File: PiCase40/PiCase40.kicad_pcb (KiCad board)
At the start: 2 copper layers, 66 x 20 mm, 3 parts, among them J1 Conn_02x20_Odd_Even_Male, J2 Conn_02x20_Odd_Even_Female, SW1 SW_MEC_5E

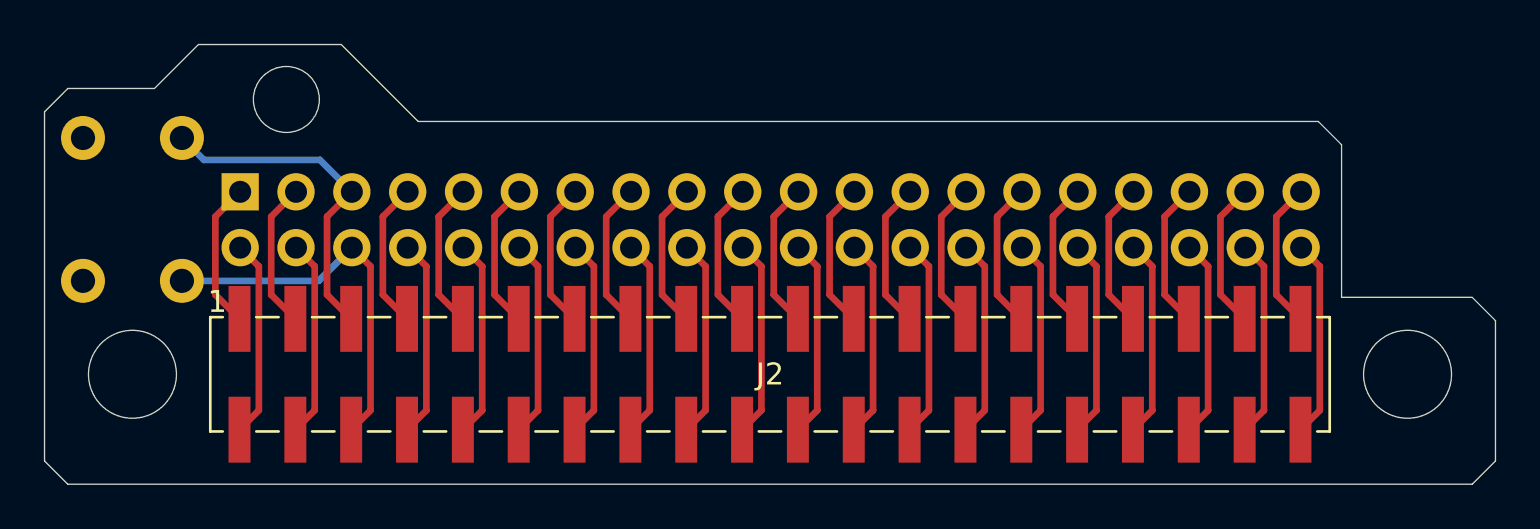
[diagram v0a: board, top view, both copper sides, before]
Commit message: Updated the PCB outline and pretified the footprints
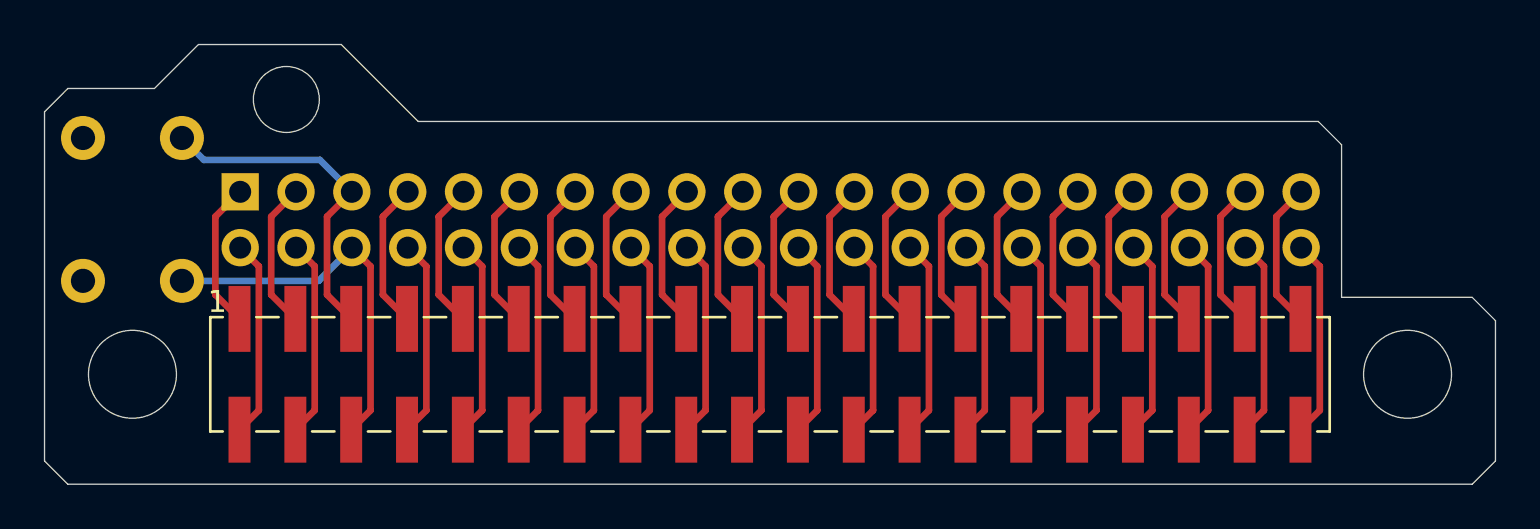
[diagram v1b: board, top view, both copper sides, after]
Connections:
- J2 pad 1: Net-(J1-Pad1) -> Net-(J2-Pad1)
- J2 pad 10: Net-(J1-Pad10) -> Net-(J2-Pad10)
- J2 pad 11: Net-(J1-Pad11) -> Net-(J2-Pad11)
- J2 pad 12: Net-(J1-Pad12) -> Net-(J2-Pad12)
- J2 pad 13: Net-(J1-Pad13) -> Net-(J2-Pad13)
- J2 pad 14: Net-(J1-Pad14) -> Net-(J2-Pad14)
- J2 pad 15: Net-(J1-Pad15) -> Net-(J2-Pad15)
- J2 pad 16: Net-(J1-Pad16) -> Net-(J2-Pad16)
- J2 pad 17: Net-(J1-Pad17) -> Net-(J2-Pad17)
- J2 pad 18: Net-(J1-Pad18) -> Net-(J2-Pad18)
- J2 pad 19: Net-(J1-Pad19) -> Net-(J2-Pad19)
- J2 pad 2: Net-(J1-Pad2) -> Net-(J2-Pad2)
- J2 pad 20: Net-(J1-Pad20) -> Net-(J2-Pad20)
- J2 pad 21: Net-(J1-Pad21) -> Net-(J2-Pad21)
- J2 pad 22: Net-(J1-Pad22) -> Net-(J2-Pad22)
- J2 pad 23: Net-(J1-Pad23) -> Net-(J2-Pad23)
- J2 pad 24: Net-(J1-Pad24) -> Net-(J2-Pad24)
- J2 pad 25: Net-(J1-Pad25) -> Net-(J2-Pad25)
- J2 pad 26: Net-(J1-Pad26) -> Net-(J2-Pad26)
- J2 pad 27: Net-(J1-Pad27) -> Net-(J2-Pad27)
- J2 pad 28: Net-(J1-Pad28) -> Net-(J2-Pad28)
- J2 pad 29: Net-(J1-Pad29) -> Net-(J2-Pad29)
- J2 pad 3: Net-(J1-Pad3) -> Net-(J2-Pad3)
- J2 pad 30: Net-(J1-Pad30) -> Net-(J2-Pad30)
- J2 pad 31: Net-(J1-Pad31) -> Net-(J2-Pad31)
- J2 pad 32: Net-(J1-Pad32) -> Net-(J2-Pad32)
- J2 pad 33: Net-(J1-Pad33) -> Net-(J2-Pad33)
- J2 pad 34: Net-(J1-Pad34) -> Net-(J2-Pad34)
- J2 pad 35: Net-(J1-Pad35) -> Net-(J2-Pad35)
- J2 pad 36: Net-(J1-Pad36) -> Net-(J2-Pad36)
- J2 pad 37: Net-(J1-Pad37) -> Net-(J2-Pad37)
- J2 pad 38: Net-(J1-Pad38) -> Net-(J2-Pad38)
- J2 pad 39: Net-(J1-Pad39) -> Net-(J2-Pad39)
- J2 pad 4: Net-(J1-Pad4) -> Net-(J2-Pad4)
- J2 pad 40: Net-(J1-Pad40) -> Net-(J2-Pad40)
- J2 pad 5: /5 -> Net-(J2-Pad5)
- J2 pad 6: /6 -> Net-(J2-Pad6)
- J2 pad 7: Net-(J1-Pad7) -> Net-(J2-Pad7)
- J2 pad 8: Net-(J1-Pad8) -> Net-(J2-Pad8)
- J2 pad 9: Net-(J1-Pad9) -> Net-(J2-Pad9)

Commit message: Prettified the PCB
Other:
- board text added: "Designed by IFo Hancroft"
